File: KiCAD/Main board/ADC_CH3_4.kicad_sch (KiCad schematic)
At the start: 149 parts, among them U34 TL072, U35 TL072, U36 LM339, U4 OPA1632DR, U5 OPA1632DR, U6 LM4562, U7 PCM1804

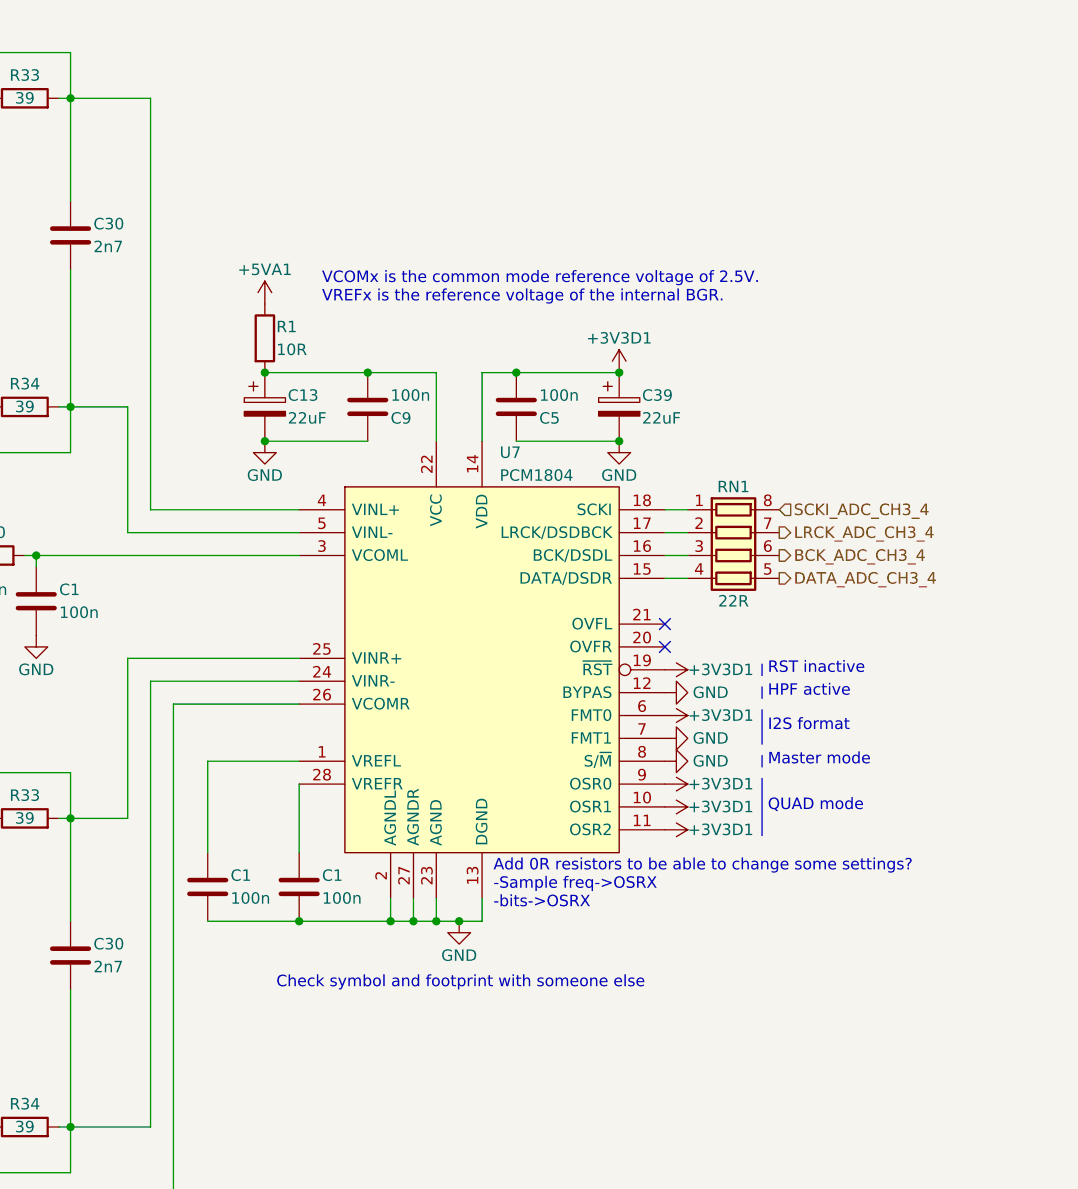
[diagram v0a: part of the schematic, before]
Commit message: Finalizer main board schematic exept passive order links. Schematic ready for review
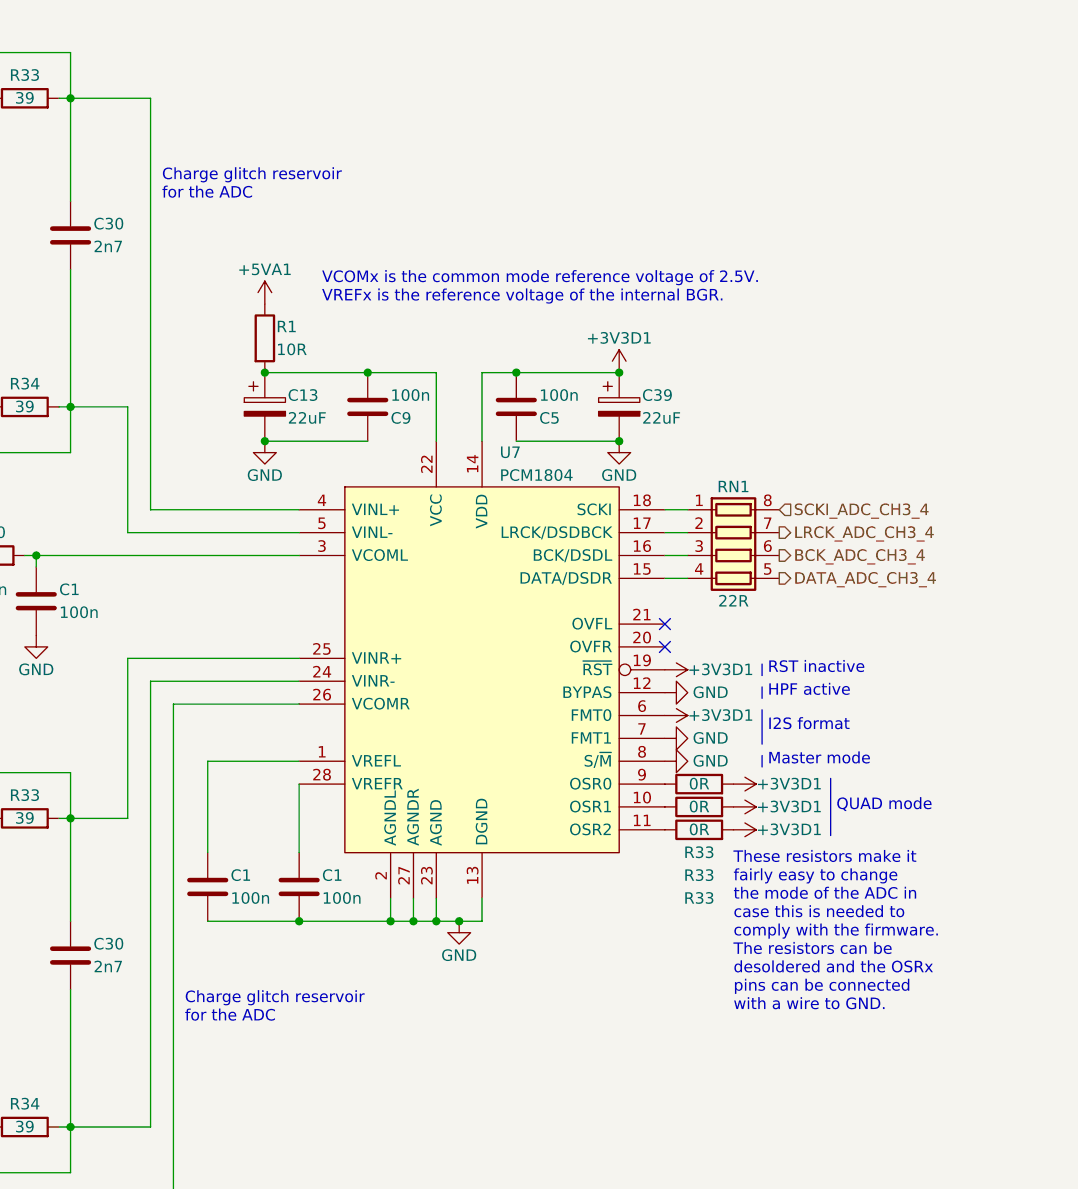
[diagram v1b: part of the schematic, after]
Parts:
- added R33 (x3): 0R, Resistor_SMD:R_0402_1005Metric, symbol Device:R
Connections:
- net +3V3D1: now also R33.2, R33.2, R33.2; no longer U7.10 (OSR1), U7.11 (OSR2), U7.9 (OSR0)
- new net: R33.1, U7.11 (OSR2)
- new net: R33.1, U7.9 (OSR0)
- new net: R33.1, U7.10 (OSR1)
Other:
- note added: "Charge glitch reservoir for the ADC"
- note added: "These resistors make it fairly easy to change the mode of the ADC in case this is needed to comply with the firmware. The resistors can be desoldered and the OSRx pins can be connected with a wire to GND."
- note removed: "Add 0R resistors to be able to change some settings? -Sample freq->OSRX -bits->OSRX"
- note removed: "Check symbol and footprint with someone else"

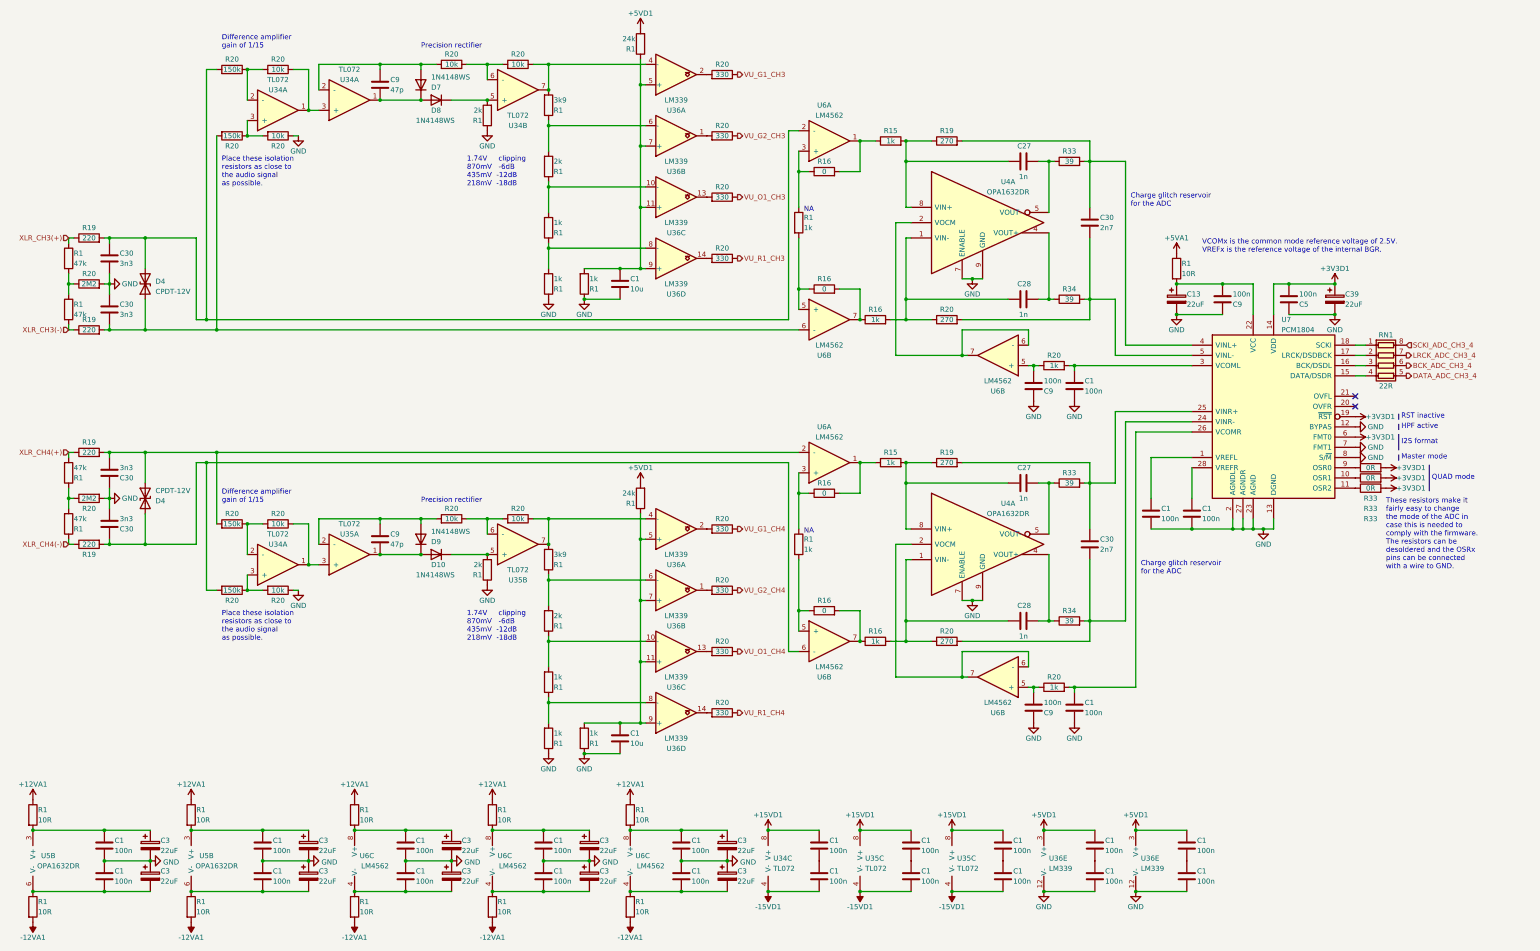
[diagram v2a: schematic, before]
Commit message: Added component links
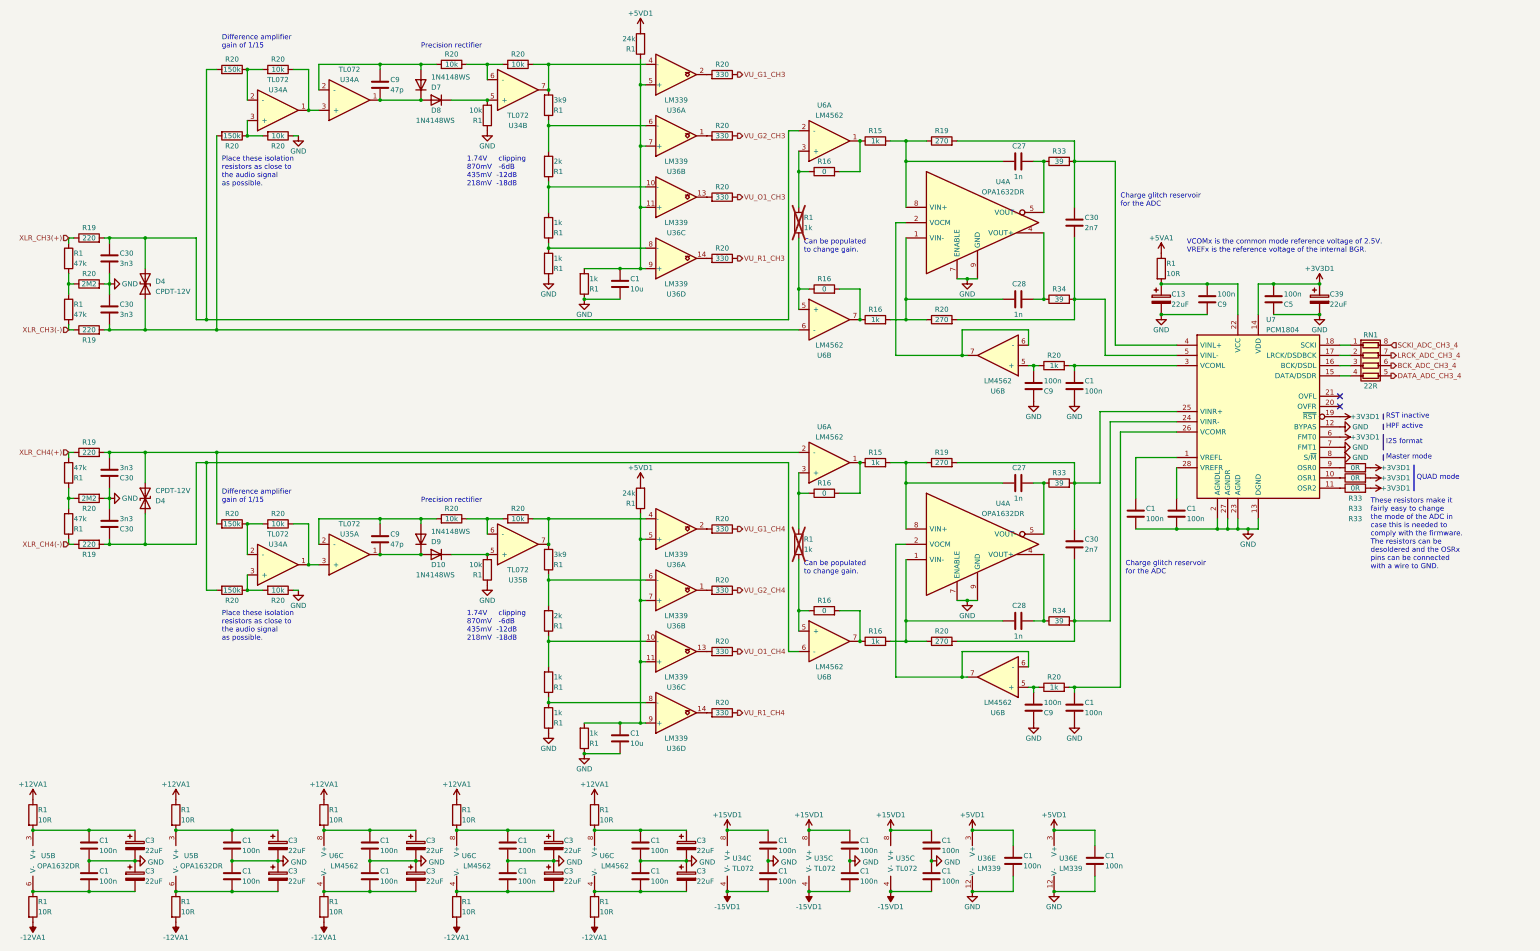
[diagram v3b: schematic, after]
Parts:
- removed C1 (x2): 100n, Capacitor_SMD:C_0402_1005Metric, symbol Device:C
- R1: value 2k -> 10k
- R1: now not fitted; now left out of the parts list
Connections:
- net GND: now also C1.1, C1.1, C1.1, C1.2, C1.2, C1.2, C1.2, C1.2
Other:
- note added: "Can be populated to change gain."
- note removed: "NA"
- moved on the sheet: C1, C13, C27, C28, C3, C30, C39, C5, C9, R1, R15, R19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
